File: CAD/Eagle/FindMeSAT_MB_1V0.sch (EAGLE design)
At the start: 129 parts, among them J291 MCX-J-P-X-RA-SM1, J685 SMA_CON, J701 MOLEX_105017-0001, J801 MICROSIM-8P_SDCARD-8P_MOLEX-1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, J901 JST_S3B-XH-A, Q101 ABS07-32.768KHZ, Q651 ABM3B-16MHZ-10-R50-1-U, U1001 CFPT-141-20MHZ, U101 ATXMEGA256A3BU-AU, U1011 OPA354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

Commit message: Eagle - USB bus lines corrected, some airwires fixed
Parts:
- removed C1091, C1092, C1093, C1094, C1095, C1096: 100nF, rcl:C-EUC0805
- added C191, C192, C193, C194, C195, C196: 100nF, rcl:C-EUC0603
- added R301: 68R, rcl:R-EU_R0603
- C1002, C1012, C1112, C1121, C711: device rcl:C-EUC0805 -> rcl:C-EUC0603
- R1013: value 10R -> 47R
- R131, R132, R141, R142, R151, R162, R163, R171, R172, R173, R221, R222, R223, R224, R231, R232, R233, R234, R241, R251: value 27R -> 68R
- RPOLY291: value 0A150 -> 50mA/150mA
- RPOLY711: value 1A0 -> 0.5A/1.0A
- RPOLY901: value 2.2A -> 1.1A/2.2A
- renumbered L1091 to L191, R152 to R151
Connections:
- new net MPU_INT: R301.1, U301.INT
- net +3V3: now also C191.1, C192.1, C193.1, C194.1, C195.1; no longer C1091.1, C1092.1, C1093.1, C1094.1, C1095.1
- net AVCC: now also C196.1; no longer C1096.1
- net GND: now also C191.2, C192.2, C193.2, C194.2, C195.2, C196.2, U501.!RESET; no longer C1091.2, C1092.2, C1093.2, C1094.2, C1095.2, C1096.2
- net I2C2_INT: now also R301.2; no longer U301.INT
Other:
- note added: "GPS active antenna"
- note added: "LITTLEFUSE 1206L005WR"
- note added: "LITTLEFUSE 1206L050YR"

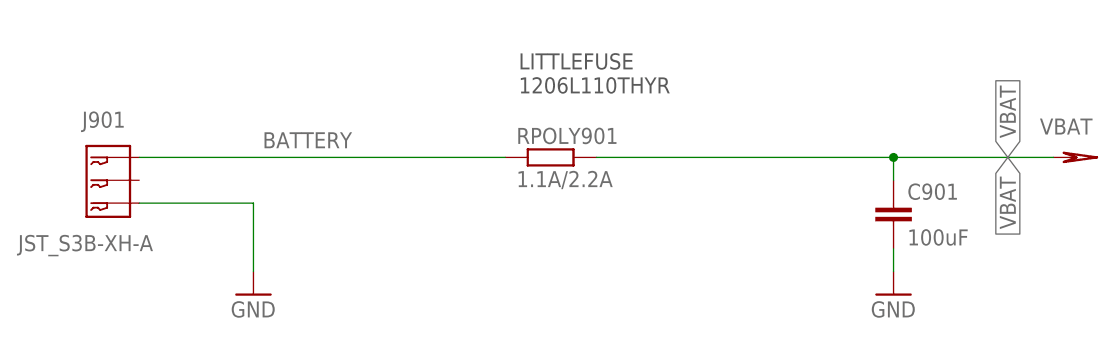
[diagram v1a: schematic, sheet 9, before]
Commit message: Eagle - Power connector mirrored, design *.dru file added
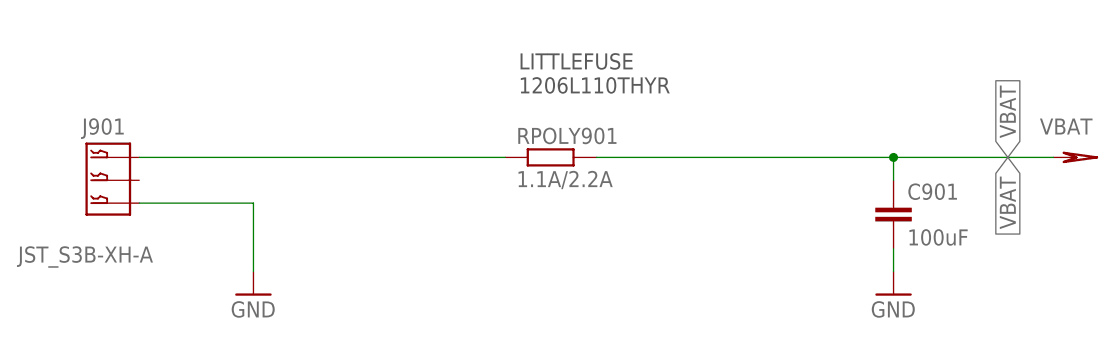
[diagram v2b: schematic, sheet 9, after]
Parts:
- RPOLY291: device rcl:R-EU_M1206 -> rcl:R-EU_R1210
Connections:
- net BATTERY: now also J901.1; no longer J901.3
- net GND: now also J901.3; no longer J901.1
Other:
- moved on the sheet: J901
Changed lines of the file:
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@@
 <part name="GND271" library="df4iah_supply" deviceset="GND" device=""/>
 <part name="GND272" library="df4iah_supply" deviceset="GND" device=""/>
-<part name="RPOLY291" library="rcl" deviceset="R-EU_" device="M1206" value="50mA/150mA"/>
+<part name="RPOLY291" library="rcl" deviceset="R-EU_" device="R1210" value="50mA/150mA"/>
 <part name="+3V3_291" library="df4iah_supply" deviceset="+3V3" device=""/>
 <part name="L291" library="rcl" deviceset="L-EU" device="L3216C" value="WE-CBF_300R"/>
@@
 <instance part="VBAT_901" gate="G$2" x="187.96" y="93.98" rot="R270"/>
 <instance part="RPOLY901" gate="G$1" x="129.54" y="93.98"/>
-<instance part="J901" gate="A" x="81.28" y="91.44" smashed="yes" rot="R180">
-<attribute name="NAME" x="77.47" y="97.282" size="1.778" layer="95" ratio="10"/>
-<attribute name="VALUE" x="70.358" y="83.566" size="1.778" layer="96" ratio="10"/>
+<instance part="J901" gate="A" x="81.28" y="91.44" smashed="yes" rot="MR0">
+<attribute name="NAME" x="77.47" y="98.298" size="1.778" layer="95" ratio="10" rot="MR180"/>
+<attribute name="VALUE" x="70.358" y="84.074" size="1.778" layer="96" ratio="10" rot="MR180"/>
 </instance>
 <instance part="C901" gate="G$1" x="167.64" y="88.9"/>
@@
 <pinref part="GND901" gate="1" pin="GND"/>
 <wire x1="96.52" y1="81.28" x2="96.52" y2="88.9" width="0.1524" layer="91"/>
+<pinref part="J901" gate="A" pin="3"/>
 <wire x1="96.52" y1="88.9" x2="83.82" y2="88.9" width="0.1524" layer="91"/>
-<pinref part="J901" gate="A" pin="1"/>
 </segment>
 <segment>
@@
 </segment>
 </net>
-<net name="BATTERY" class="1">
+<net name="BATTERY" class="0">
 <segment>
 <pinref part="RPOLY901" gate="G$1" pin="1"/>
+<pinref part="J901" gate="A" pin="1"/>
 <wire x1="124.46" y1="93.98" x2="83.82" y2="93.98" width="0.1524" layer="91"/>
-<label x="97.536" y="94.996" size="1.778" layer="95"/>
-<pinref part="J901" gate="A" pin="3"/>
-</segment>
-</net>
+</segment>
+</net>

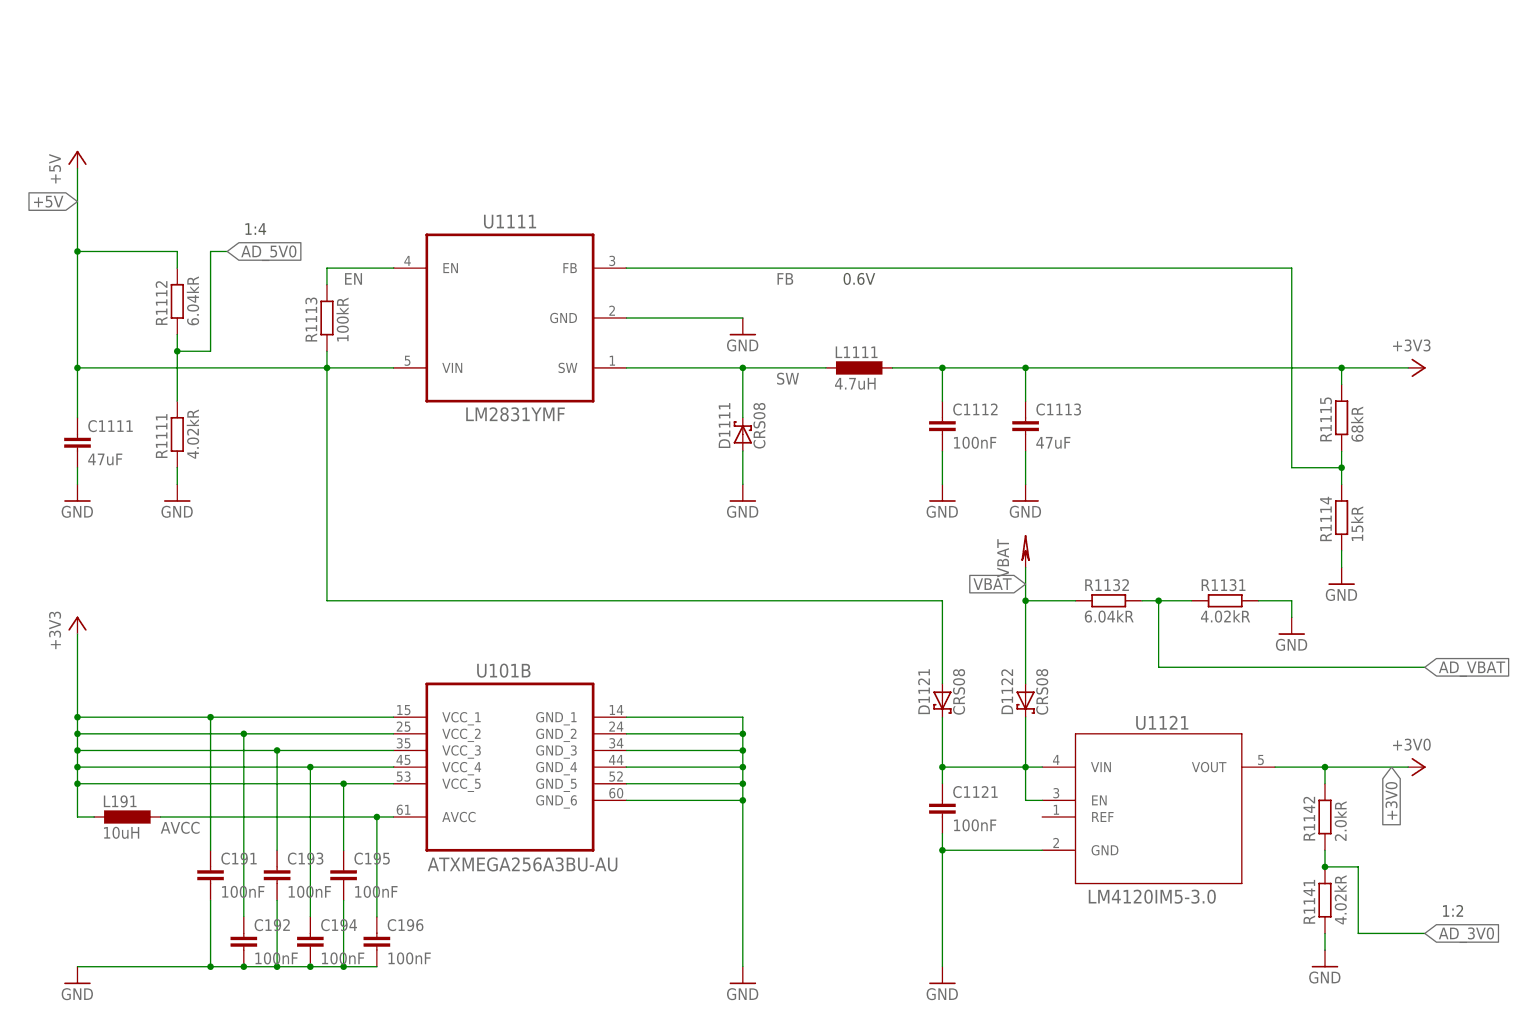
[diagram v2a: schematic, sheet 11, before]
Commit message: Eagle - power for 3.3V from common rail of 5V and battery
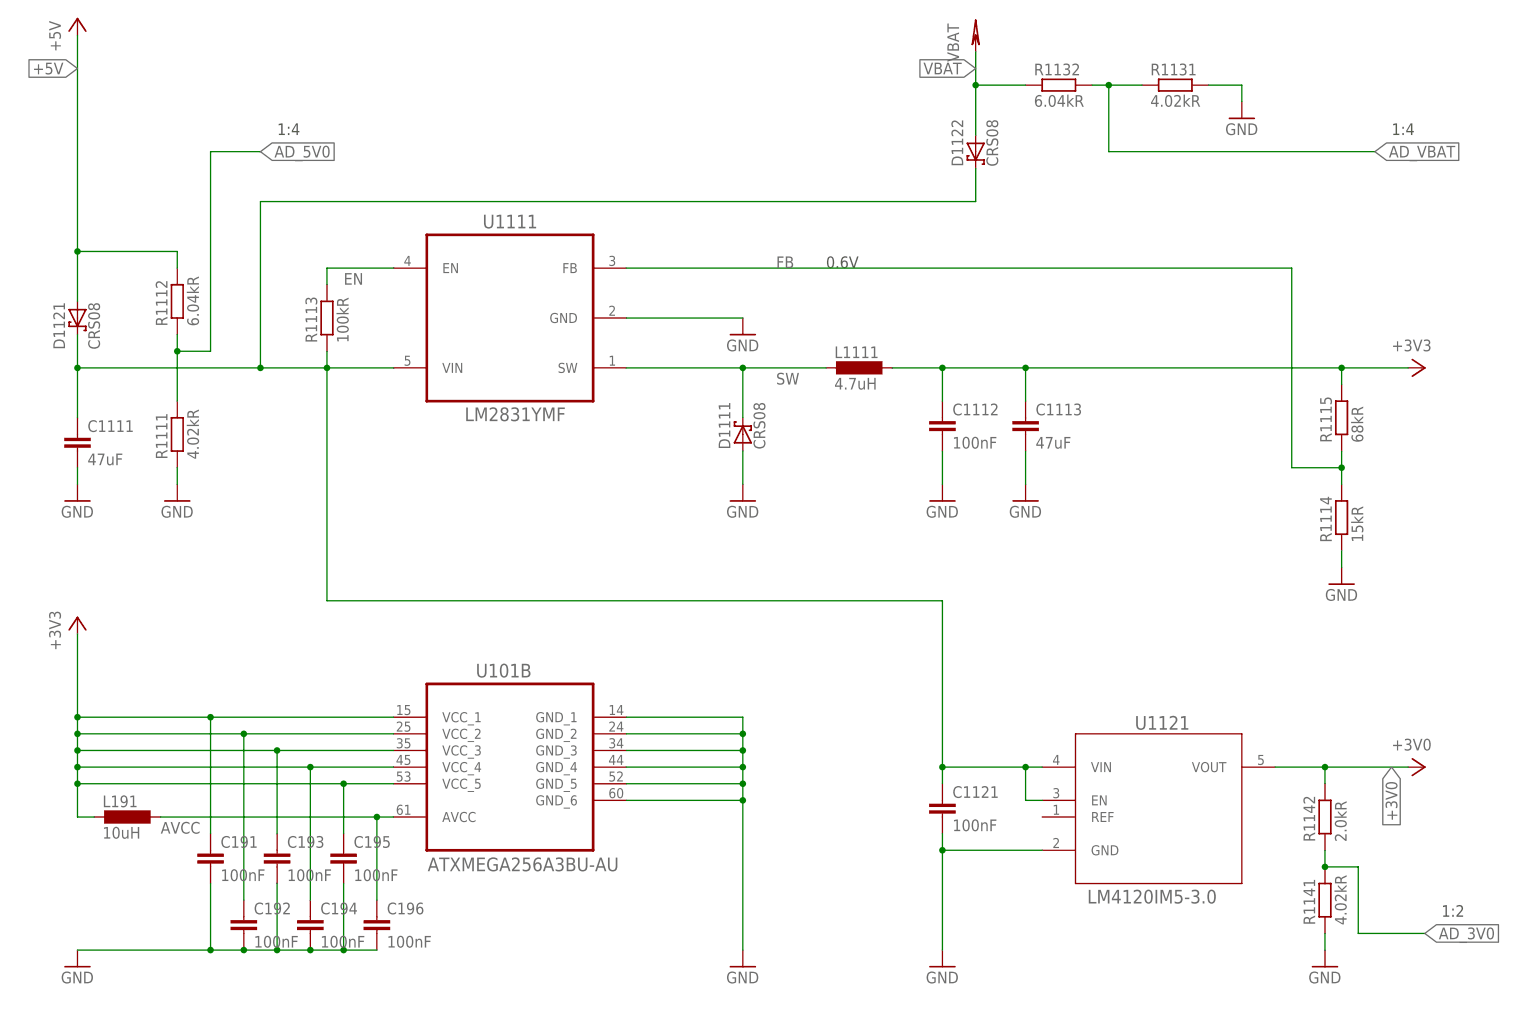
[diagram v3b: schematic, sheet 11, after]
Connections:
- removed net VBAT_DD: C1121.1, D1121.C, D1122.C, U1121.EN, U1121.VIN
- new net VIN: C1111.1, C1121.1, D1121.C, D1122.C, R1113.1, U1111.VIN, U1121.EN, U1121.VIN
- net +5V: no longer C1111.1, R1113.1, U1111.VIN
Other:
- moved on the sheet: C101, C191, C192, C193, C194, C195, C196, D1121, D1122, R1131, R1132

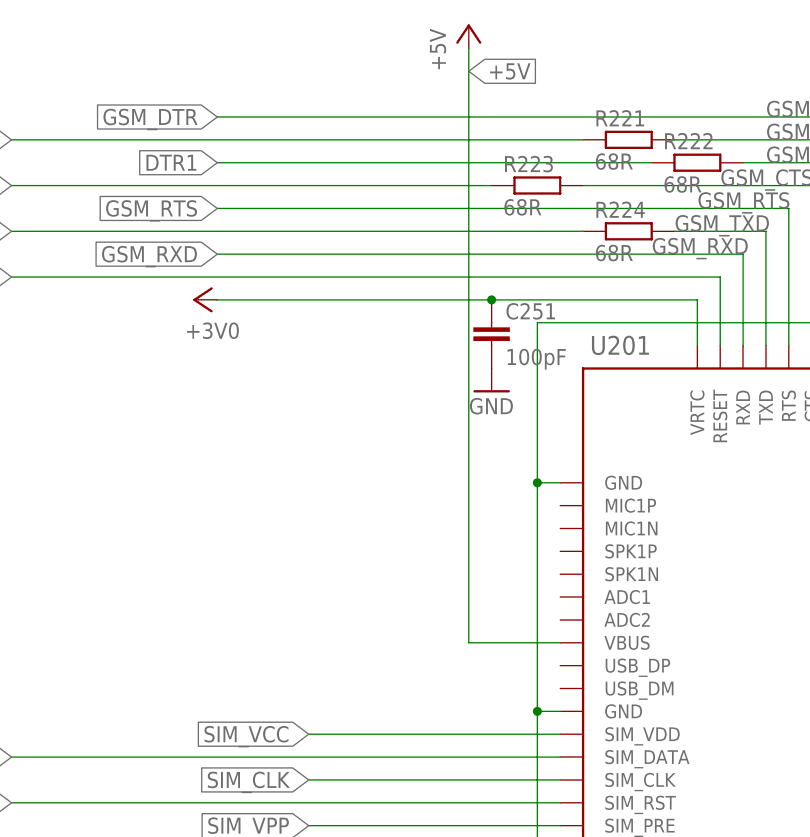
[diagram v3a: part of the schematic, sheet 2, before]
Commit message: Eagle - power jumper for SIM808 added
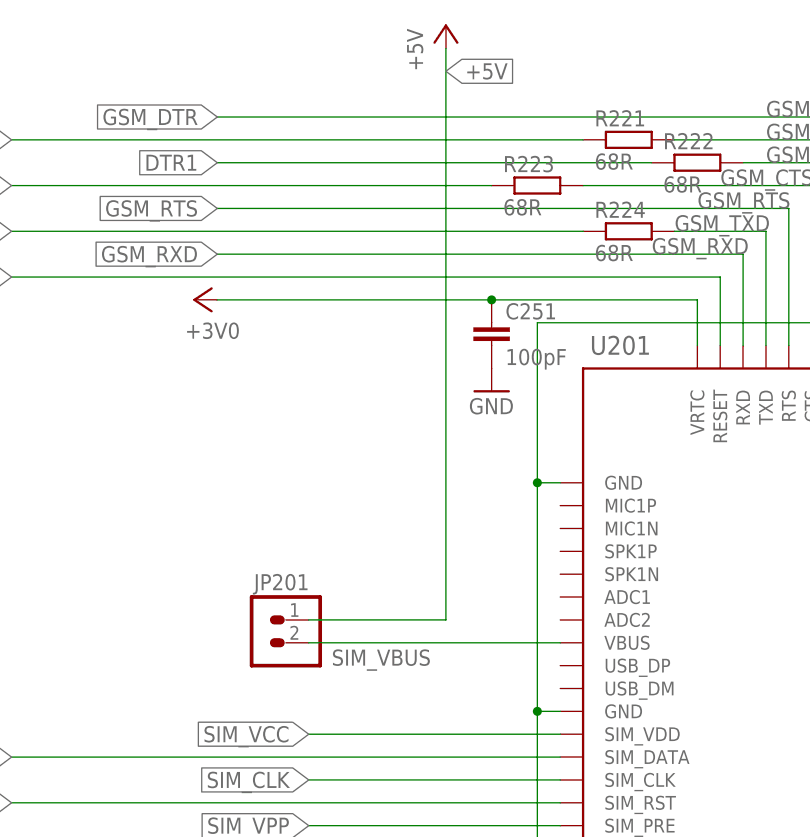
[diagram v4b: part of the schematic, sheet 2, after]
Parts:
- added JP201: POW, df4iah_connector:HEADER-1X2
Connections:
- new net SIM_VBUS: JP201.2, U201.VBUS
- net +5V: now also JP201.1; no longer U201.VBUS
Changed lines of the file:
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@@
 <part name="+3V3_1" library="df4iah_supply" deviceset="+3V3" device=""/>
 <part name="R301" library="rcl" deviceset="R-EU_" device="R0603" value="68R"/>
+<part name="JP201" library="df4iah_connector" deviceset="HEADER-1X2" device="" value="POW"/>
 </parts>
 <sheets>
@@
 <attribute name="VALUE" x="151.384" y="140.081" size="1.778" layer="96"/>
 </instance>
-<instance part="+5V0_201" gate="G$1" x="83.82" y="170.18"/>
+<instance part="+5V0_201" gate="G$1" x="81.28" y="170.18"/>
 <instance part="R211" gate="G$1" x="78.74" y="50.8"/>
 <instance part="R212" gate="G$1" x="78.74" y="43.18"/>
@@
 <instance part="R241" gate="G$1" x="195.58" y="96.52"/>
 <instance part="R251" gate="G$1" x="96.52" y="35.56"/>
+<instance part="JP201" gate="A" x="63.5" y="104.14" smashed="yes" rot="MR0">
+<attribute name="NAME" x="59.944" y="109.22" size="1.778" layer="95" ratio="10" rot="MR180"/>
+</instance>
 </instances>
 <busses>
@@
 <segment>
 <pinref part="+5V0_201" gate="G$1" pin="+5V"/>
-<pinref part="U201" gate="G$1" pin="VBUS"/>
-<wire x1="83.82" y1="167.64" x2="83.82" y2="101.6" width="0.1524" layer="91"/>
-<wire x1="83.82" y1="101.6" x2="93.98" y2="101.6" width="0.1524" layer="91"/>
-<label x="83.82" y="165.1" size="1.778" layer="95" xref="yes"/>
+<wire x1="81.28" y1="167.64" x2="81.28" y2="104.14" width="0.1524" layer="91"/>
+<label x="81.28" y="165.1" size="1.778" layer="95" xref="yes"/>
+<pinref part="JP201" gate="A" pin="1"/>
+<wire x1="81.28" y1="104.14" x2="66.04" y2="104.14" width="0.1524" layer="91"/>
 </segment>
 </net>
@@
 </segment>
 </net>
+<net name="SIM_VBUS" class="0">
+<segment>
+<pinref part="U201" gate="G$1" pin="VBUS"/>
+<wire x1="93.98" y1="101.6" x2="66.04" y2="101.6" width="0.1524" layer="91"/>
+<pinref part="JP201" gate="A" pin="2"/>
+<label x="68.58" y="99.06" size="1.778" layer="95"/>
+</segment>
+</net>
